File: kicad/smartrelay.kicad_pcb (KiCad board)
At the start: 2 copper layers, 84.5 x 61 mm, 41 parts, among them J1 OSTYK42103030, J2 CONN_01X03, J3 CONN_01X03, Q1 2N3904, Q2 2N3904, Q3 2N3904, Q4 2N3904, Q5 2N3904, Q6 2N3904, Q7 2N3904, U1 TSOP38338, U2 MCP16251T-I/CH, U3 ArduinoNano

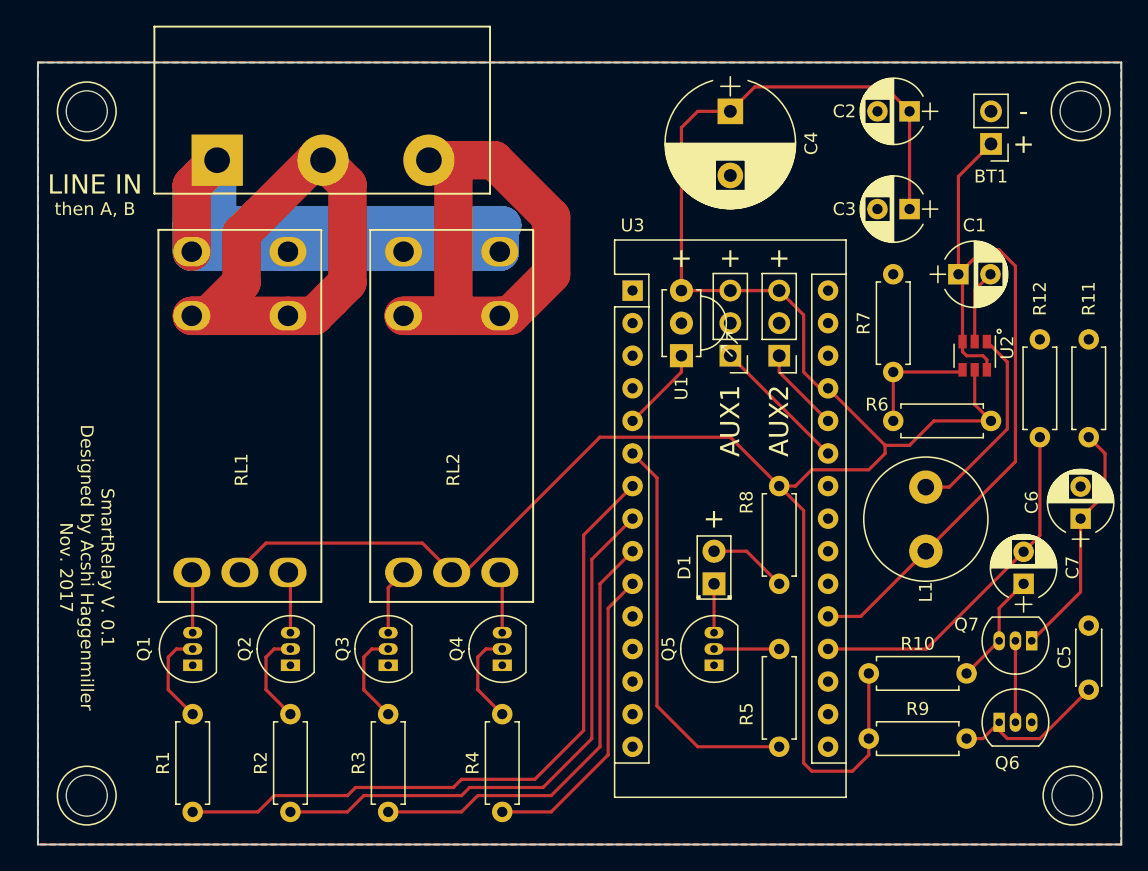
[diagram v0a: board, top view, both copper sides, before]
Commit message: smart relay redesign with smd and without arduino nano
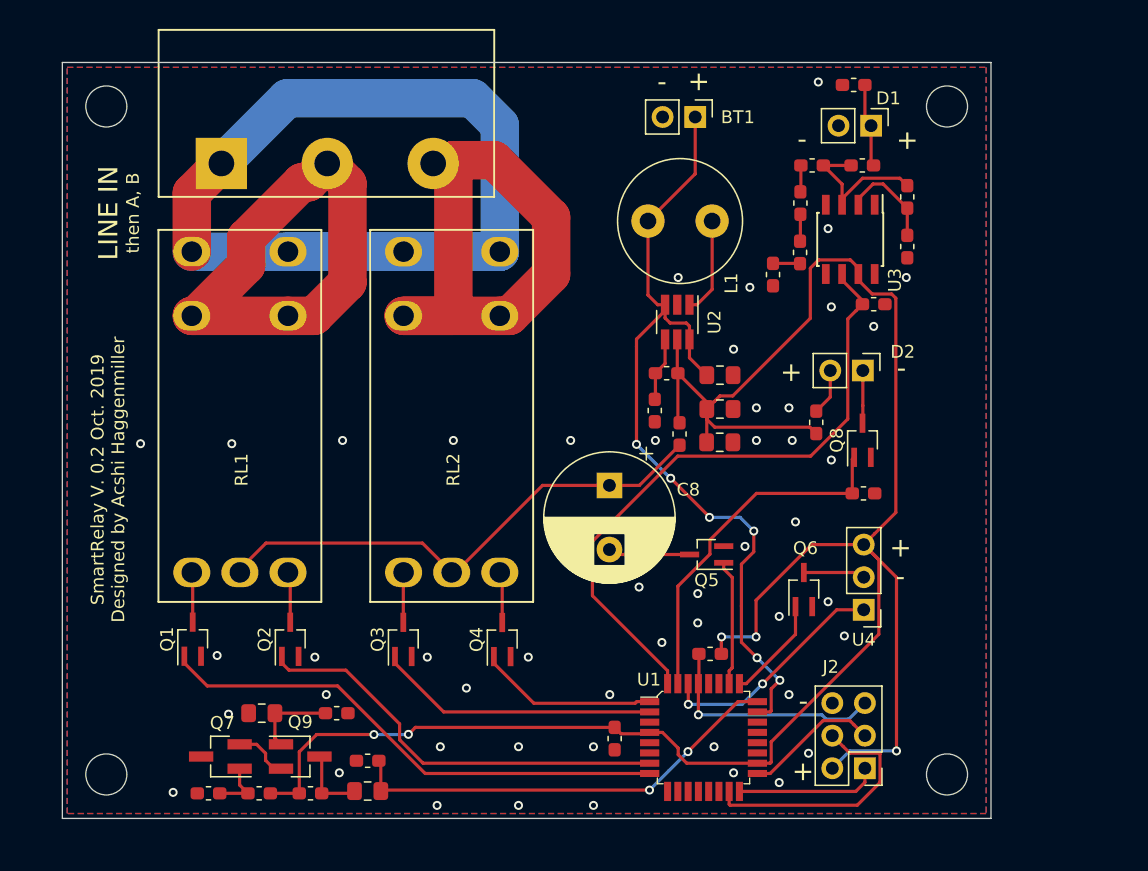
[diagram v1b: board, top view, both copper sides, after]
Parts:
- removed J3: CONN_01X03, Pin_Headers:Pin_Header_Straight_1x03_Pitch2.54mm
- removed the REF** at (181.6, 139.7)
- removed the REF** at (182.2, 86.4)
- removed the REF** at (104.8, 139.7)
- removed the REF** at (104.8, 86.4)
- added C10: 10uF, Capacitor_SMD:C_0805_2012Metric_Pad1.15x1.40mm_HandSolder, F.Cu at (118.4, 133.3)
- added C11: 10uF, Capacitor_SMD:C_0805_2012Metric_Pad1.15x1.40mm_HandSolder, F.Cu at (126.7, 139.3)
- added C8: 2200uF, Capacitor_THT:CP_Radial_D10.0mm_P5.00mm, F.Cu at (145.5, 115.5)
- added C9: 100nF, Capacitor_SMD:C_0603_1608Metric_Pad1.05x0.95mm_HandSolder, F.Cu at (114.3, 139.5)
- added D2: IR1503, Connector_PinHeader_2.54mm:PinHeader_1x02_P2.54mm_Vertical, F.Cu at (165.3, 106.6)
- added Q8: 2N7002WT1G, Package_TO_SOT_SMD:SOT-323_SC-70_Handsoldering, F.Cu at (165.2, 112.0)
- added Q9: MMBT3904, Package_TO_SOT_SMD:SOT-23_Handsoldering, F.Cu at (121.4, 136.7)
- added R13: 3.9R, Resistor_SMD:R_0603_1608Metric_Pad1.05x0.95mm_HandSolder, F.Cu at (161.6, 110.6)
- added R14: 4.7k, Resistor_SMD:R_0603_1608Metric_Pad1.05x0.95mm_HandSolder, F.Cu at (122.2, 139.5)
- added R15: 1k, Resistor_SMD:R_0603_1608Metric_Pad1.05x0.95mm_HandSolder, F.Cu at (124.3, 133.3)
- added R16: 100k, Resistor_SMD:R_0603_1608Metric_Pad1.05x0.95mm_HandSolder, F.Cu at (126.7, 137.0)
- added REF**: MountingHole_3.2mm_M3, MountingHole:MountingHole_3.2mm_M3, F.Cu at (171.8, 138.0)
- added REF**: MountingHole_3.2mm_M3, MountingHole:MountingHole_3.2mm_M3, F.Cu at (106.3, 138.0)
- added REF**: MountingHole_3.2mm_M3, MountingHole:MountingHole_3.2mm_M3, F.Cu at (171.8, 86.0)
- added REF**: MountingHole_3.2mm_M3, MountingHole:MountingHole_3.2mm_M3, F.Cu at (106.3, 86.0)
- added U4: TSOP38338, Connector_PinHeader_2.54mm:PinHeader_1x03_P2.54mm_Vertical, F.Cu at (165.3, 125.2)
- BT1: footprint Pin_Headers:Pin_Header_Straight_1x02_Pitch2.54mm -> Connector_PinHeader_2.54mm:PinHeader_1x02_P2.54mm_Vertical
- C1: value 4.7uF -> 100nF; footprint Capacitors_THT:CP_Radial_D5.0mm_P2.50mm -> Capacitor_SMD:C_0603_1608Metric_Pad1.05x0.95mm_HandSolder
- C2: value 10uF -> 4.7uF; footprint Capacitors_THT:CP_Radial_D5.0mm_P2.50mm -> Capacitor_SMD:C_0805_2012Metric_Pad1.15x1.40mm_HandSolder
- C3: value 10uF -> 0.15nF; footprint Capacitors_THT:CP_Radial_D5.0mm_P2.50mm -> Capacitor_SMD:C_0603_1608Metric_Pad1.05x0.95mm_HandSolder
- C4: value 2200uF -> 100nF; footprint Capacitors_THT:CP_Radial_D10.0mm_P5.00mm -> Capacitor_SMD:C_0603_1608Metric_Pad1.05x0.95mm_HandSolder
- C5: footprint Capacitors_THT:C_Disc_D4.3mm_W1.9mm_P5.00mm -> Capacitor_SMD:C_0603_1608Metric_Pad1.05x0.95mm_HandSolder
- C6, C7: footprint Capacitors_THT:CP_Radial_D5.0mm_P2.50mm -> Capacitor_SMD:C_0805_2012Metric_Pad1.15x1.40mm_HandSolder
- D1: value IR1503 -> D_Photo; footprint LEDs:LED_D2.0mm_W4.8mm_H2.5mm_FlatTop -> Connector_PinHeader_2.54mm:PinHeader_1x02_P2.54mm_Vertical
- J2: value CONN_01X03 -> AVR-ISP-6; footprint Pin_Headers:Pin_Header_Straight_1x03_Pitch2.54mm -> Connector_PinHeader_2.54mm:PinHeader_2x03_P2.54mm_Vertical
- L1: footprint Inductors_THT:L_Radial_D9.5mm_P5.00mm_Fastron_07HVP -> Inductor_THT:L_Radial_D9.5mm_P5.00mm_Fastron_07HVP
- Q1, Q2, Q3, Q4, Q5, Q6: value 2N3904 -> 2N7002WT1G; footprint TO_SOT_Packages_THT:TO-92_Inline_Narrow_Oval -> Package_TO_SOT_SMD:SOT-323_SC-70_Handsoldering
- Q7: value 2N3904 -> MMBT3904; footprint TO_SOT_Packages_THT:TO-92_Inline_Narrow_Oval -> Package_TO_SOT_SMD:SOT-23_Handsoldering
- R1: value 1k -> 10k; footprint Resistors_THT:R_Axial_DIN0207_L6.3mm_D2.5mm_P7.62mm_Horizontal -> Resistor_SMD:R_0603_1608Metric_Pad1.05x0.95mm_HandSolder
- R10: value 4.7k -> 47R; footprint Resistors_THT:R_Axial_DIN0207_L6.3mm_D2.5mm_P7.62mm_Horizontal -> Resistor_SMD:R_0603_1608Metric_Pad1.05x0.95mm_HandSolder
- R11: footprint Resistors_THT:R_Axial_DIN0207_L6.3mm_D2.5mm_P7.62mm_Horizontal -> Resistor_SMD:R_0603_1608Metric_Pad1.05x0.95mm_HandSolder
- R12: value 100k -> 680k; footprint Resistors_THT:R_Axial_DIN0207_L6.3mm_D2.5mm_P7.62mm_Horizontal -> Resistor_SMD:R_0603_1608Metric_Pad1.05x0.95mm_HandSolder
- R2: value 1k -> 1M; footprint Resistors_THT:R_Axial_DIN0207_L6.3mm_D2.5mm_P7.62mm_Horizontal -> Resistor_SMD:R_0603_1608Metric_Pad1.05x0.95mm_HandSolder
- R3, R4, R5: value 1k -> 22M; footprint Resistors_THT:R_Axial_DIN0207_L6.3mm_D2.5mm_P7.62mm_Horizontal -> Resistor_SMD:R_0603_1608Metric_Pad1.05x0.95mm_HandSolder
- R6: value 3.09M -> 22M; footprint Resistors_THT:R_Axial_DIN0207_L6.3mm_D2.5mm_P7.62mm_Horizontal -> Resistor_SMD:R_0603_1608Metric_Pad1.05x0.95mm_HandSolder
- R7: value 1M -> 470k; footprint Resistors_THT:R_Axial_DIN0207_L6.3mm_D2.5mm_P7.62mm_Horizontal -> Resistor_SMD:R_0603_1608Metric_Pad1.05x0.95mm_HandSolder
- R8: value 62R -> 3.09M; footprint Resistors_THT:R_Axial_DIN0207_L6.3mm_D2.5mm_P7.62mm_Horizontal -> Resistor_SMD:R_0603_1608Metric_Pad1.05x0.95mm_HandSolder
- R9: value 680k -> 1M; footprint Resistors_THT:R_Axial_DIN0207_L6.3mm_D2.5mm_P7.62mm_Horizontal -> Resistor_SMD:R_0603_1608Metric_Pad1.05x0.95mm_HandSolder
- U1: value TSOP38338 -> ATMEGA328PB-AU; footprint Opto-Devices:IRReceiver_Vishay_MINICAST-3pin -> digikey-footprints:TQFP-32_7x7mm
- U2: footprint TO_SOT_Packages_SMD:SOT-23-6 -> Package_TO_SOT_SMD:SOT-23-6_Handsoldering
- U3: value ArduinoNano -> MAX918ESA; footprint Modules:Arduino_Nano -> Package_SO:SOIC-8_3.9x4.9mm_P1.27mm
- moved R2 71.7 mm to (164.6, 84.3), turned to 180 degrees
- moved R12 66.9 mm to (118.2, 139.5), turned to 180 degrees
- moved Q7 63.9 mm to (115.2, 136.7)
- moved R3 60.3 mm to (161.3, 90.6), turned to 180 degrees
- moved R4 52.8 mm to (160.4, 93.5), turned to 270 degrees
- moved C1 45.0 mm to (145.9, 135.3), turned to 270 degrees
- moved R1 42.2 mm to (153.4, 128.7), turned to 180 degrees
- moved D1 37.8 mm to (165.9, 87.5), turned to 270 degrees
- moved C5 34.4 mm to (166.1, 101.4), turned to 0 degrees
- moved L1 33.6 mm to (148.5, 94.9), turned to 0 degrees
- moved J2 32.8 mm to (165.4, 137.6)
- moved R5 31.0 mm to (160.4, 97.4)
- moved R9 30.5 mm to (149.1, 109.7), turned to 270 degrees
- moved U1 29.8 mm to (152.8, 135.2), turned to 0 degrees
- moved C6 29.4 mm to (154.1, 109.6), turned to 0 degrees
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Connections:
- C1 pad 1: /+1.2V -> +5V
- C2 pad 1: +5V -> /+1.2V
- C3 pad 1: +5V -> Net-(C3-Pad1)
- C3 pad 2: GND -> Net-(C3-Pad2)
- C4 pad 1: +5V -> Net-(C4-Pad1)
- C5 pad 1: Net-(C5-Pad1) -> /WAKEUP
- C6 pad 1: Net-(C6-Pad1) -> +5V
- C7 pad 1: Net-(C7-Pad1) -> +5V
- C7 pad 2: /NOISE -> GND
- D1 pad 1: Net-(D1-Pad1) -> Net-(C3-Pad2)
- D1 pad 2: Net-(D1-Pad2) -> GND
- J2 pad 1: /AUX1 -> /MISO
- J2 pad 2: GND -> +5V
- J2 pad 3: +5V -> /SCK
- Q1 pad 1: GND -> /RELAY_CTRL_A_RESET
- Q1 pad 2: Net-(Q1-Pad2) -> GND
- Q2 pad 1: GND -> /RELAY_CTRL_A_SET
- Q2 pad 2: Net-(Q2-Pad2) -> GND
- Q3 pad 1: GND -> /RELAY_CTRL_B_RESET
- Q3 pad 2: Net-(Q3-Pad2) -> GND
- Q4 pad 1: GND -> /RELAY_CTRL_B_SET
- Q4 pad 2: Net-(Q4-Pad2) -> GND
- Q5 pad 1: GND -> /CAP_ENABLE
- Q5 pad 2: Net-(Q5-Pad2) -> GND
- Q5 pad 3: Net-(D1-Pad1) -> Net-(C8-Pad2)
- Q6 pad 1: Net-(C5-Pad1) -> /RECV_ENABLE
- Q6 pad 2: Net-(Q6-Pad2) -> GND
- Q7 pad 1: Net-(C6-Pad1) -> Net-(C9-Pad1)
- Q7 pad 2: Net-(Q6-Pad2) -> Net-(Q7-Pad2)
- Q7 pad 3: Net-(C7-Pad1) -> (no net)
- R1 pad 1: /RELAY_CTRL_A_RESET -> +5V
- R1 pad 2: Net-(Q1-Pad2) -> /~RST
- R10 pad 2: Net-(C7-Pad1) -> /+5V_RELAY
- R11 pad 1: Net-(C6-Pad1) -> (no net)
- R11 pad 2: GND -> /IR_SEND
- R12 pad 1: /NOISE -> +5V
- R12 pad 2: GND -> Net-(C9-Pad1)
- R2 pad 1: /RELAY_CTRL_A_SET -> Net-(C3-Pad2)
- R2 pad 2: Net-(Q2-Pad2) -> GND
- R3 pad 1: /RELAY_CTRL_B_RESET -> Net-(C3-Pad1)
- R3 pad 2: Net-(Q3-Pad2) -> Net-(R3-Pad2)
- R4 pad 1: /RELAY_CTRL_B_SET -> Net-(R3-Pad2)
- R4 pad 2: Net-(Q4-Pad2) -> Net-(R4-Pad2)
- R5 pad 1: Net-(Q5-Pad2) -> Net-(R4-Pad2)
- R5 pad 2: /IR_SEND -> Net-(R5-Pad2)
- R6 pad 1: +5V -> Net-(R5-Pad2)
- R6 pad 2: Net-(R6-Pad2) -> GND
- R7 pad 1: Net-(R6-Pad2) -> Net-(C4-Pad1)
- R7 pad 2: GND -> Net-(C3-Pad1)
- R8 pad 2: Net-(D1-Pad2) -> Net-(R8-Pad2)
- R9 pad 1: +5V -> Net-(R8-Pad2)
- R9 pad 2: Net-(C5-Pad1) -> GND
- RL1 pad 5: +5V -> /+5V_RELAY
- RL2 pad 5: +5V -> /+5V_RELAY
- U1 pad 1: /IR_RECV -> /RELAY_CTRL_B_SET
- U1 pad 2: GND -> /RELAY_CTRL_B_RESET
- U1 pad 3: +5V -> (no net)
- U2 pad 4: Net-(R6-Pad2) -> Net-(R8-Pad2)
- U3 pad 1: Net-(U3-Pad1) -> (no net)
- U3 pad 2: Net-(U3-Pad2) -> Net-(C4-Pad1)
- U3 pad 3: Net-(U3-Pad3) -> Net-(C3-Pad1)
- U3 pad 5: /IR_RECV -> (no net)
- U3 pad 6: /IR_SEND -> /WAKEUP
- U3 pad 7: /RELAY_CTRL_A_RESET -> +5V
- U3 pad 8: /RELAY_CTRL_A_SET -> (no net)
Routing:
- net /WAKEUP: track 0.00 -> 49.8 mm
- net /+5V_RELAY: track 0.00 -> 41.4 mm
- net /MOSI: track 0.00 -> 20.0 mm
- net Net-(C6-Pad1): track 18.8 -> 0.00 mm
- net /~RST: track 0.00 -> 18.4 mm, vias 0 -> 1
- net /RELAY_CTRL_A_RESET: track 53.7 -> 40.4 mm
- net /RELAY_CTRL_B_RESET: track 34.9 -> 21.9 mm
- net Net-(C5-Pad1): track 12.5 -> 0.00 mm
- net Net-(C3-Pad1): track 0.00 -> 12.3 mm
- net /IR_RECV: track 6.66 -> 18.4 mm, vias 0 -> 2
- net /RELAY_CTRL_A_SET: track 44.3 -> 33.1 mm
- net /MISO: track 0.00 -> 11.2 mm
- net /AUX2: track 10.8 -> 0.00 mm
- net /SCK: track 0.00 -> 10.6 mm
- net /LiveIn: track 93.3 -> 82.9 mm
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- added copper zone on F.Cu, net GND
- removed copper zone on F.Cu, net +5V
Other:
- board size 84.5 x 61 mm -> 72.4 x 58.9 mm
- net class Default: via_dia 0.6 -> 0.7
- rule pad_to_mask_clearance: 0.2 -> 0.06
- rule trace_min: 0.2 -> 0.15
- board text added: "SmartRelay V. 0.2 Oct. 2019 Designed by Acshi Haggenmiller"
- board text removed: "AUX1"
- board text removed: "AUX2"
- board text removed: "SmartRelay V. 0.1 Designed by Acshi Haggenmiller Nov. 2017"
